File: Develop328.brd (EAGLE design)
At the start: 100 x 80 mm, 11 parts

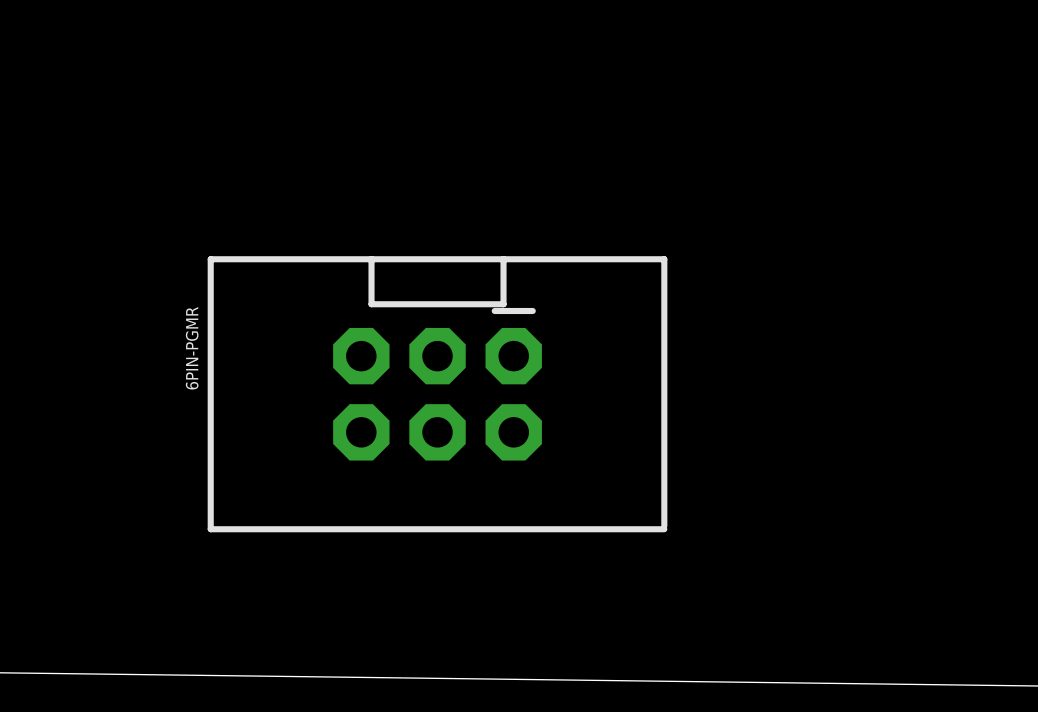
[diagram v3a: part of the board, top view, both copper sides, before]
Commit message: Added GND and VCC nets and wired up the 6 pin programmer
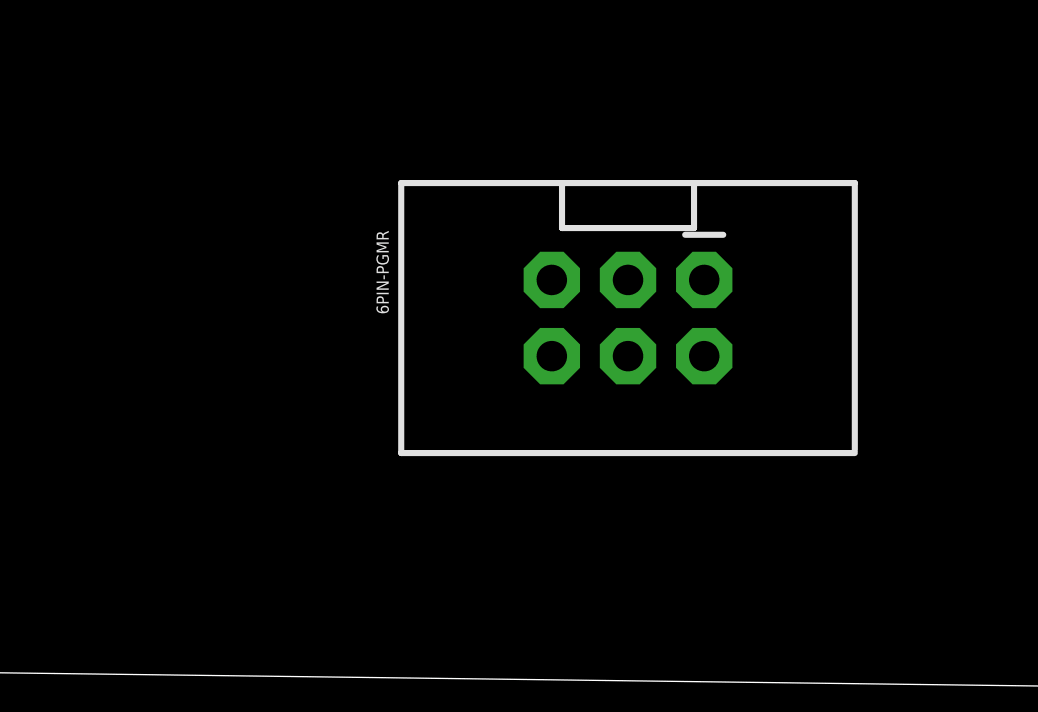
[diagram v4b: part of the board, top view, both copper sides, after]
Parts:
- moved 6PIN-PGMR 6.84 mm to (52.1, 12.7)
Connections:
- removed net AVCC: MICROCONTROLLER.20
- new net GND: 6PIN-PGMR.2, GND_HDR.1, GND_HDR.2, MICROCONTROLLER.22, MICROCONTROLLER.8
- new net N$25: MICROCONTROLLER.20, VCC-HDR.1
- net N$10: now also 6PIN-PGMR.3
- net N$11: now also 6PIN-PGMR.5
- net N$12: now also 6PIN-PGMR.4
- net N$15: now also 6PIN-PGMR.1
- net VCC: now also 6PIN-PGMR.6, VCC-HDR.2
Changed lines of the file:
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@@
 <element name="5V-DC-JACK" library="adafruit" package="PJ-102A" value="" x="88.9" y="78.74"/>
 <element name="PWR-LED" library="adafruit" package="LED3MM" value="" x="77.47" y="73.66"/>
-<element name="6PIN-PGMR" library="SparkFun-Connectors" package="2X3-SHROUDED" value="" x="45.72" y="10.16" rot="R270">
-<attribute name="PROD_ID" value="CONN-10681" x="45.72" y="10.16" size="1.778" layer="27" rot="R270" display="off"/>
+<element name="6PIN-PGMR" library="SparkFun-Connectors" package="2X3-SHROUDED" value="" x="52.07" y="12.7" rot="R270">
+<attribute name="PROD_ID" value="CONN-10681" x="52.07" y="12.7" size="1.778" layer="27" rot="R270" display="off"/>
 </element>
 <element name="PORTD-HDR" library="SparkFun-Connectors" package="1X08_ROUND" value="" x="77.47" y="66.04" rot="R270">
@@
 <signal name="VCC">
 <contactref element="MICROCONTROLLER" pad="7"/>
-</signal>
-<signal name="AVCC">
-<contactref element="MICROCONTROLLER" pad="20"/>
+<contactref element="6PIN-PGMR" pad="6"/>
+<contactref element="VCC-HDR" pad="2"/>
+<wire x1="11.43" y1="68.58" x2="43.18" y2="50.8" width="0" layer="19" extent="1-1"/>
+<wire x1="49.53" y1="11.43" x2="43.18" y2="50.8" width="0" layer="19" extent="1-1"/>
 </signal>
 <signal name="N$1">
@@
 <contactref element="PORTC-HDR" pad="2"/>
 <contactref element="MICROCONTROLLER" pad="24"/>
+<contactref element="6PIN-PGMR" pad="3"/>
+<wire x1="52.07" y1="13.97" x2="77.47" y2="30.48" width="0" layer="19" extent="1-1"/>
 <wire x1="50.8" y1="55.88" x2="77.47" y2="30.48" width="0" layer="19" extent="1-1"/>
 </signal>
@@
 <contactref element="PORTC-HDR" pad="3"/>
 <contactref element="MICROCONTROLLER" pad="25"/>
+<contactref element="6PIN-PGMR" pad="5"/>
+<wire x1="49.53" y1="13.97" x2="77.47" y2="33.02" width="0" layer="19" extent="1-1"/>
 <wire x1="50.8" y1="58.42" x2="77.47" y2="33.02" width="0" layer="19" extent="1-1"/>
 </signal>
@@
 <contactref element="PORTC-HDR" pad="4"/>
 <contactref element="MICROCONTROLLER" pad="26"/>
+<contactref element="6PIN-PGMR" pad="4"/>
+<wire x1="52.07" y1="11.43" x2="77.47" y2="35.56" width="0" layer="19" extent="1-1"/>
 <wire x1="50.8" y1="60.96" x2="77.47" y2="35.56" width="0" layer="19" extent="1-1"/>
 </signal>
@@
 <contactref element="PORTC-HDR" pad="7"/>
 <contactref element="MICROCONTROLLER" pad="1"/>
+<contactref element="6PIN-PGMR" pad="1"/>
+<wire x1="54.61" y1="13.97" x2="77.47" y2="43.18" width="0" layer="19" extent="1-1"/>
 <wire x1="43.18" y1="66.04" x2="77.47" y2="43.18" width="0" layer="19" extent="1-1"/>
 </signal>
@@
 <wire x1="11.43" y1="53.34" x2="50.8" y2="48.26" width="0" layer="19" extent="1-1"/>
 </signal>
+<signal name="GND">
+<contactref element="6PIN-PGMR" pad="2"/>
+<contactref element="GND_HDR" pad="2"/>
+<contactref element="GND_HDR" pad="1"/>
+<contactref element="MICROCONTROLLER" pad="8"/>
+<contactref element="MICROCONTROLLER" pad="22"/>
+<wire x1="43.18" y1="48.26" x2="50.8" y2="50.8" width="0" layer="19" extent="1-1"/>
+<wire x1="11.43" y1="59.69" x2="43.18" y2="48.26" width="0" layer="19" extent="1-1"/>
+<wire x1="11.43" y1="62.23" x2="11.43" y2="59.69" width="0" layer="19" extent="1-1"/>
+<wire x1="54.61" y1="11.43" x2="43.18" y2="48.26" width="0" layer="19" extent="1-1"/>
+</signal>
+<signal name="N$25">
+<contactref element="VCC-HDR" pad="1"/>
+<contactref element="MICROCONTROLLER" pad="20"/>
+<wire x1="11.43" y1="66.04" x2="50.8" y2="45.72" width="0" layer="19" extent="1-1"/>
+</signal>
 </signals>

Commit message: Wired capacitor and led to vcc and gnd
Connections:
- net GND: now also PWR-LED.K, VCC_CAP.2
- net VCC: now also PWR-LED.A, VCC_CAP.1
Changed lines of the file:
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@@
 <contactref element="6PIN-PGMR" pad="6"/>
 <contactref element="VCC-HDR" pad="2"/>
+<contactref element="VCC_CAP" pad="1"/>
+<contactref element="PWR-LED" pad="A"/>
+<wire x1="43.18" y1="50.8" x2="76.2" y2="73.66" width="0" layer="19" extent="1-1"/>
 <wire x1="11.43" y1="68.58" x2="43.18" y2="50.8" width="0" layer="19" extent="1-1"/>
 <wire x1="49.53" y1="11.43" x2="43.18" y2="50.8" width="0" layer="19" extent="1-1"/>
+<wire x1="-34.87" y1="-38.1" x2="49.53" y2="11.43" width="0" layer="19" extent="1-1"/>
 </signal>
 <signal name="N$1">
@@
 <contactref element="MICROCONTROLLER" pad="8"/>
 <contactref element="MICROCONTROLLER" pad="22"/>
+<contactref element="VCC_CAP" pad="2"/>
+<contactref element="PWR-LED" pad="K"/>
+<wire x1="50.8" y1="50.8" x2="78.74" y2="73.66" width="0" layer="19" extent="1-1"/>
 <wire x1="43.18" y1="48.26" x2="50.8" y2="50.8" width="0" layer="19" extent="1-1"/>
 <wire x1="11.43" y1="59.69" x2="43.18" y2="48.26" width="0" layer="19" extent="1-1"/>
 <wire x1="11.43" y1="62.23" x2="11.43" y2="59.69" width="0" layer="19" extent="1-1"/>
 <wire x1="54.61" y1="11.43" x2="43.18" y2="48.26" width="0" layer="19" extent="1-1"/>
+<wire x1="-33.71" y1="-38.1" x2="54.61" y2="11.43" width="0" layer="19" extent="1-1"/>
 </signal>
 <signal name="N$25">

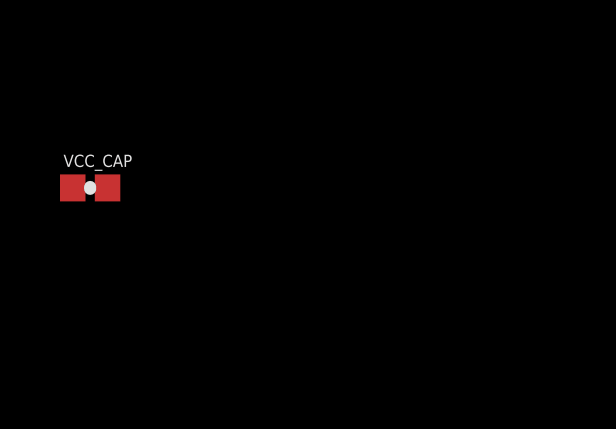
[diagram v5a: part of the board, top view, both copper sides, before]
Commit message: Wired up the input jack and rewired the vcc pin filter
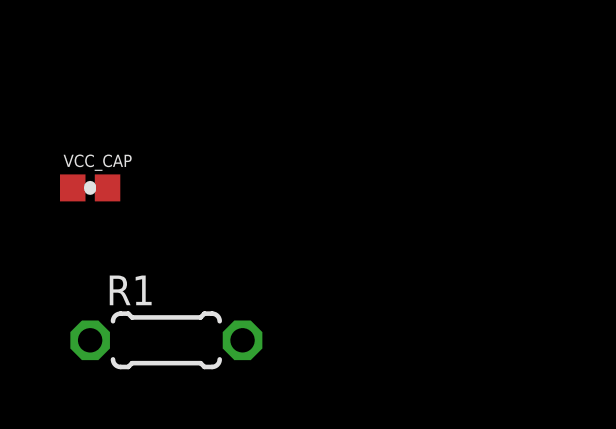
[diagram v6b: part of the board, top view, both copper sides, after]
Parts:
- added R1: 200ohm, resistor:0204/5
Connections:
- new net N$26: 5V-DC-JACK.RING, PWR-LED.A
- new net N$27: PWR-LED.K, R1.2
- net GND: now also 5V-DC-JACK.RING_SW, R1.1; no longer PWR-LED.K
- net VCC: now also 5V-DC-JACK.TIP; no longer PWR-LED.A
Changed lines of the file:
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@@
 <attribute name="PROD_ID" value="CAP-12416" x="-34.29" y="-38.1" size="1.778" layer="27" display="off"/>
 </element>
+<element name="R1" library="resistor" package="0204/5" value="200ohm" x="-31.75" y="-43.18"/>
 </elements>
 <signals>
@@
 <contactref element="6PIN-PGMR" pad="6"/>
 <contactref element="VCC-HDR" pad="2"/>
+<contactref element="5V-DC-JACK" pad="TIP"/>
 <contactref element="VCC_CAP" pad="1"/>
-<contactref element="PWR-LED" pad="A"/>
-<wire x1="43.18" y1="50.8" x2="76.2" y2="73.66" width="0" layer="19" extent="1-1"/>
+<wire x1="43.18" y1="50.8" x2="89" y2="69.45" width="0" layer="19" extent="1-1"/>
 <wire x1="11.43" y1="68.58" x2="43.18" y2="50.8" width="0" layer="19" extent="1-1"/>
 <wire x1="49.53" y1="11.43" x2="43.18" y2="50.8" width="0" layer="19" extent="1-1"/>
@@
 <contactref element="MICROCONTROLLER" pad="22"/>
 <contactref element="VCC_CAP" pad="2"/>
-<contactref element="PWR-LED" pad="K"/>
-<wire x1="50.8" y1="50.8" x2="78.74" y2="73.66" width="0" layer="19" extent="1-1"/>
+<contactref element="5V-DC-JACK" pad="RING_SW"/>
+<contactref element="R1" pad="1"/>
+<wire x1="50.8" y1="50.8" x2="84.3" y2="72.45" width="0" layer="19" extent="1-1"/>
 <wire x1="43.18" y1="48.26" x2="50.8" y2="50.8" width="0" layer="19" extent="1-1"/>
 <wire x1="11.43" y1="59.69" x2="43.18" y2="48.26" width="0" layer="19" extent="1-1"/>
@@
 <wire x1="54.61" y1="11.43" x2="43.18" y2="48.26" width="0" layer="19" extent="1-1"/>
 <wire x1="-33.71" y1="-38.1" x2="54.61" y2="11.43" width="0" layer="19" extent="1-1"/>
+<wire x1="-34.29" y1="-43.18" x2="-33.71" y2="-38.1" width="0" layer="19" extent="1-1"/>
 </signal>
 <signal name="N$25">
@@
 <wire x1="11.43" y1="66.04" x2="50.8" y2="45.72" width="0" layer="19" extent="1-1"/>
 </signal>
+<signal name="N$26">
+<contactref element="5V-DC-JACK" pad="RING"/>
+<contactref element="PWR-LED" pad="A"/>
+<wire x1="76.2" y1="73.66" x2="89" y2="75.35" width="0" layer="19" extent="1-1"/>
+</signal>
+<signal name="N$27">
+<contactref element="PWR-LED" pad="K"/>
+<contactref element="R1" pad="2"/>
+<wire x1="-29.21" y1="-43.18" x2="78.74" y2="73.66" width="0" layer="19" extent="1-1"/>
+</signal>
 </signals>

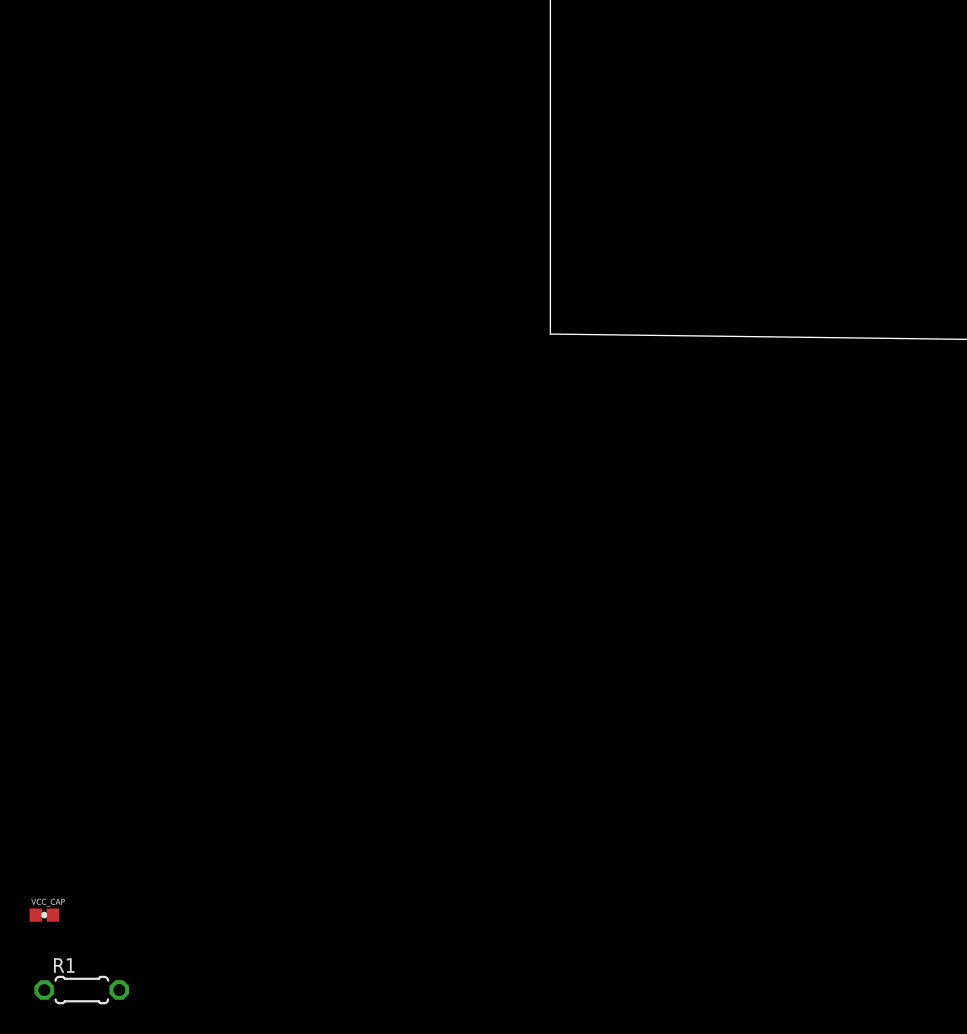
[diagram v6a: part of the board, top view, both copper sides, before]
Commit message: Changed capacitor out for through hole style
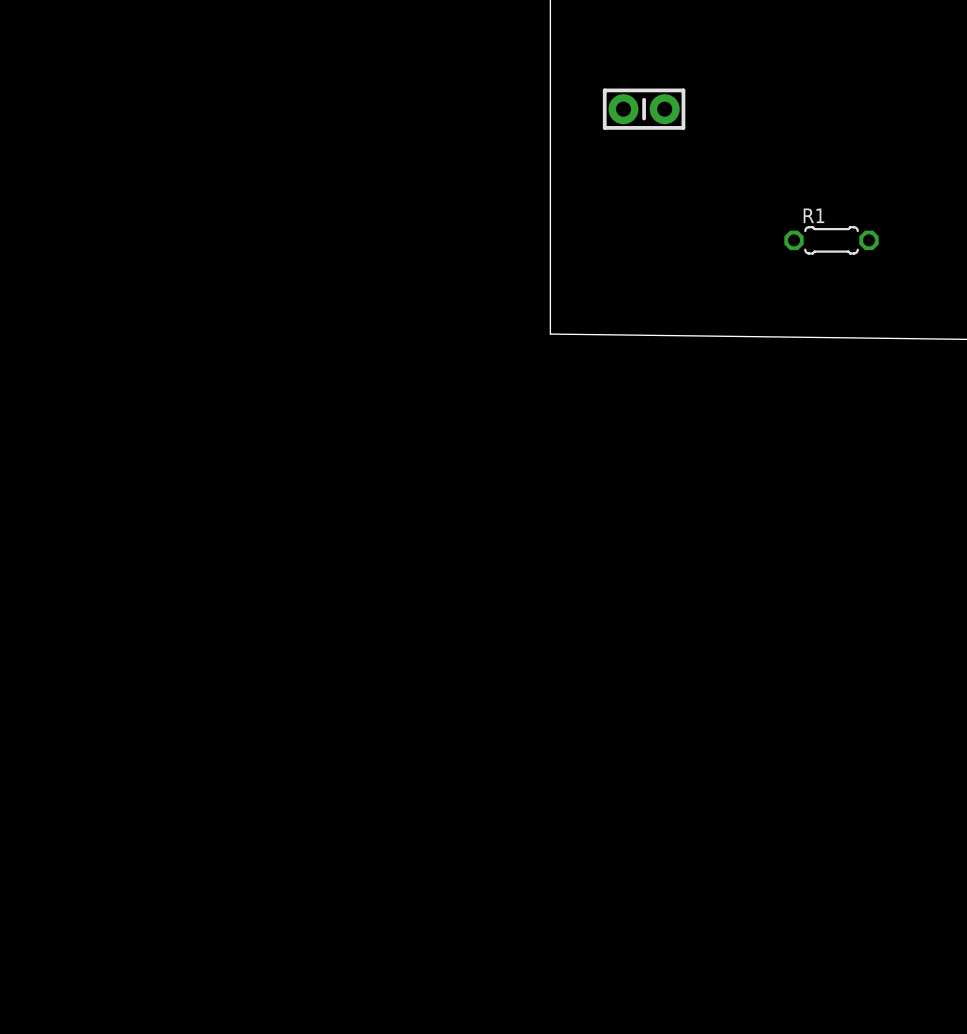
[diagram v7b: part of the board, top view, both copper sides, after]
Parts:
- VCC_CAP: device SparkFun-Capacitors:0402-CAP -> SparkFun-Capacitors:CAP-PTH-SMALL-KIT
- moved R1 71.8 mm to (19.1, 7.62)
- moved VCC_CAP 68.1 mm to (6.35, 16.5)
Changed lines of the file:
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@@
 <element name="VCC-HDR" library="SparkFun-Connectors" package="1X02" value="" x="11.43" y="66.04" rot="R90"/>
 <element name="AREF-HDR" library="SparkFun-Connectors" package="1X01" value="" x="11.43" y="53.34"/>
-<element name="VCC_CAP" library="SparkFun-Capacitors" package="0402-CAP" value="0.1uF" x="-34.29" y="-38.1">
-<attribute name="PROD_ID" value="CAP-12416" x="-34.29" y="-38.1" size="1.778" layer="27" display="off"/>
+<element name="VCC_CAP" library="SparkFun-Capacitors" package="CAP-PTH-SMALL-KIT" value="0.1uF" x="6.35" y="16.51">
+<attribute name="PROD_ID" value="CAP-08370" x="6.35" y="16.51" size="1.778" layer="27" display="off"/>
 </element>
-<element name="R1" library="resistor" package="0204/5" value="200ohm" x="-31.75" y="-43.18"/>
+<element name="R1" library="resistor" package="0204/5" value="200ohm" x="19.05" y="7.62"/>
 </elements>
 <signals>
@@
 <wire x1="11.43" y1="68.58" x2="43.18" y2="50.8" width="0" layer="19" extent="1-1"/>
 <wire x1="49.53" y1="11.43" x2="43.18" y2="50.8" width="0" layer="19" extent="1-1"/>
-<wire x1="-34.87" y1="-38.1" x2="49.53" y2="11.43" width="0" layer="19" extent="1-1"/>
+<wire x1="4.953" y1="16.51" x2="49.53" y2="11.43" width="0" layer="19" extent="1-1"/>
 </signal>
 <signal name="N$1">
@@
 <wire x1="11.43" y1="62.23" x2="11.43" y2="59.69" width="0" layer="19" extent="1-1"/>
 <wire x1="54.61" y1="11.43" x2="43.18" y2="48.26" width="0" layer="19" extent="1-1"/>
-<wire x1="-33.71" y1="-38.1" x2="54.61" y2="11.43" width="0" layer="19" extent="1-1"/>
-<wire x1="-34.29" y1="-43.18" x2="-33.71" y2="-38.1" width="0" layer="19" extent="1-1"/>
+<wire x1="7.747" y1="16.51" x2="54.61" y2="11.43" width="0" layer="19" extent="1-1"/>
+<wire x1="16.51" y1="7.62" x2="7.747" y2="16.51" width="0" layer="19" extent="1-1"/>
 </signal>
 <signal name="N$25">
@@
 <contactref element="PWR-LED" pad="K"/>
 <contactref element="R1" pad="2"/>
-<wire x1="-29.21" y1="-43.18" x2="78.74" y2="73.66" width="0" layer="19" extent="1-1"/>
+<wire x1="21.59" y1="7.62" x2="78.74" y2="73.66" width="0" layer="19" extent="1-1"/>
 </signal>
 </signals>
